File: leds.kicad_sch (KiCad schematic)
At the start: 61 parts, among them U14 ADUM1201ARZ-RL7

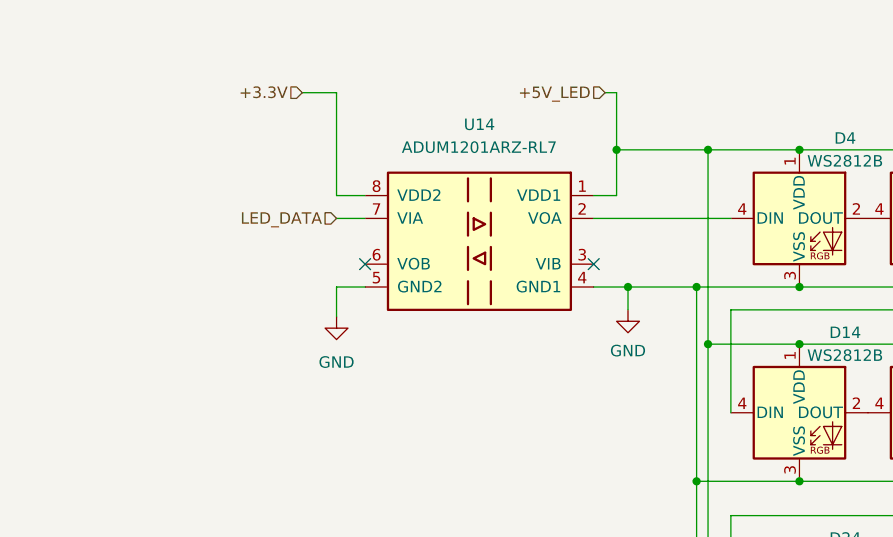
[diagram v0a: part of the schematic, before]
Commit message: bypass caps for digital isolators
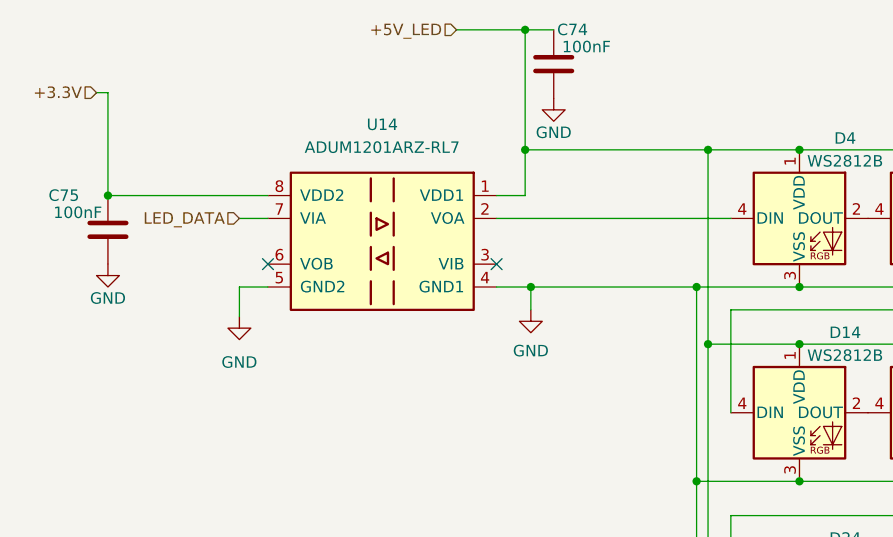
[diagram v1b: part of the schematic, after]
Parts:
- added C74, C75: 100nF, Capacitor_SMD:C_0402_1005Metric, symbol Device:C
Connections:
- net +3.3V: now also C75.2
- net +5V_LED: now also C74.2
- net GND: now also C74.1, C75.1
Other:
- moved on the sheet: U14

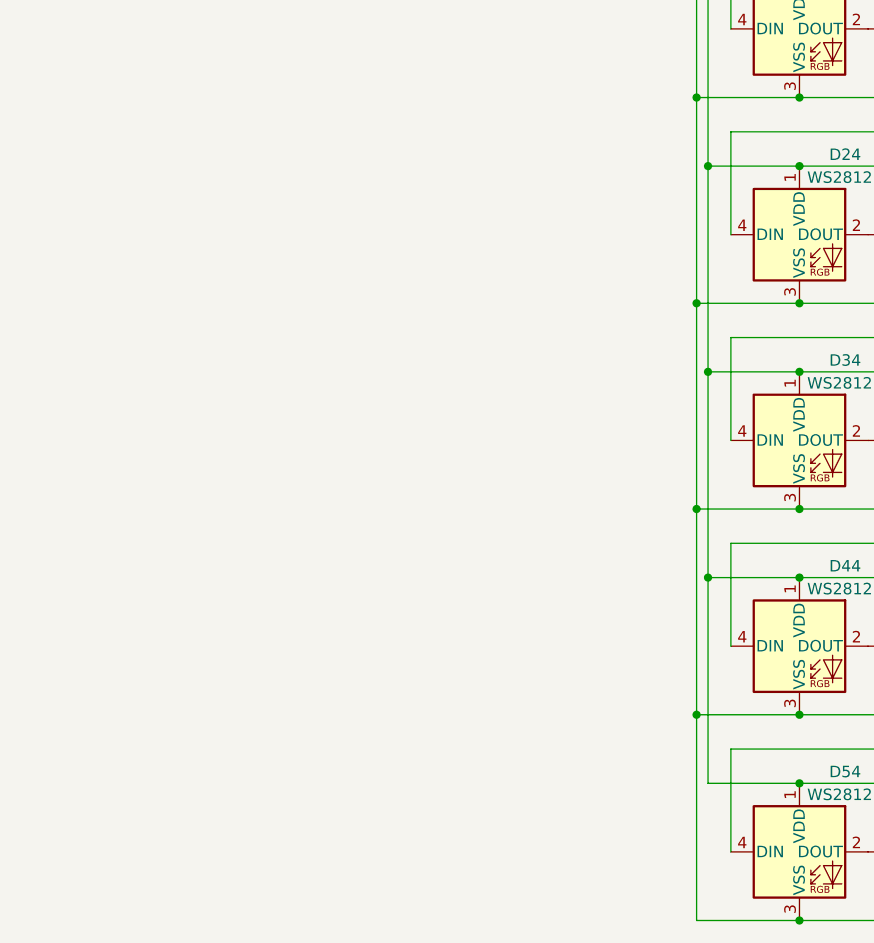
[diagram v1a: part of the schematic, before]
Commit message: first round of routing completed, led capacitors added to schematics
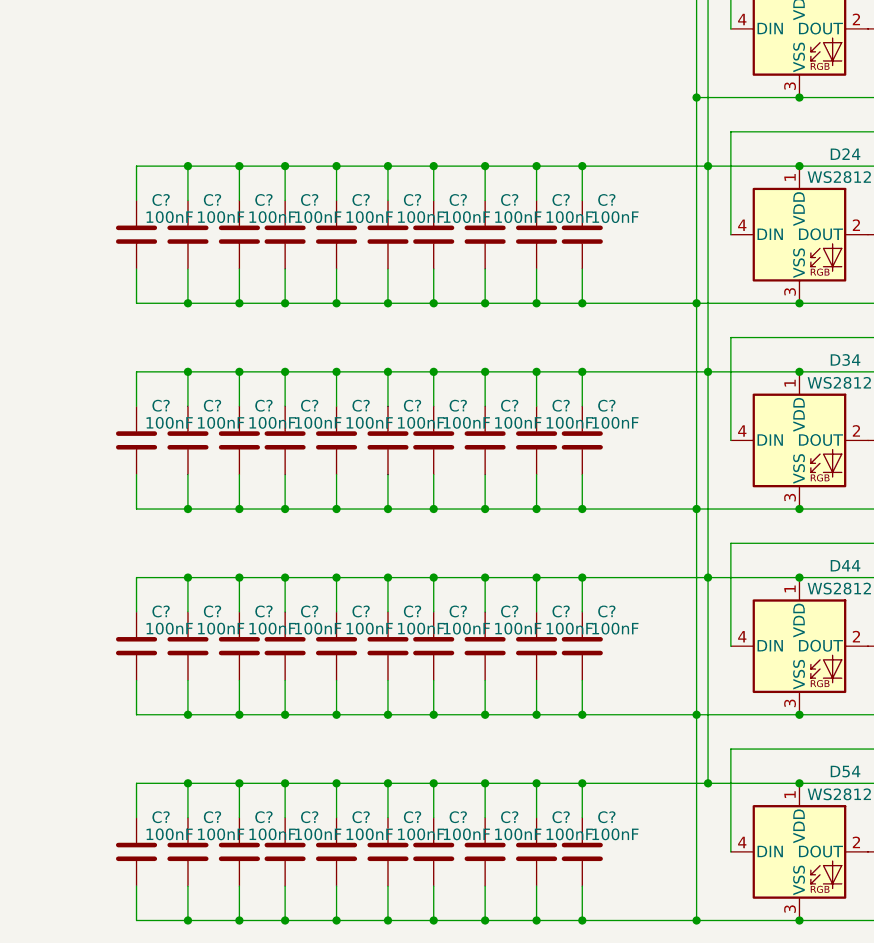
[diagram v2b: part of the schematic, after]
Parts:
- added C? (x40): 100nF, Capacitor_SMD:C_0402_1005Metric, symbol Device:C
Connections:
- net +5V_LED: now also C?.2, C?.2, C?.2, C?.2, C?.2, C?.2, C?.2, C?.2, C?.2, C?.2, C?.2, C?.2, C?.2, C?.2, C?.2, C?.2, C?.2, C?.2, C?.2, C?.2, C?.2, C?.2, C?.2, C?.2, C?.2, C?.2, C?.2, C?.2, C?.2, C?.2, C?.2, C?.2, C?.2, C?.2, C?.2, C?.2, C?.2, C?.2, C?.2, C?.2
- net GND: now also C?.1, C?.1, C?.1, C?.1, C?.1, C?.1, C?.1, C?.1, C?.1, C?.1, C?.1, C?.1, C?.1, C?.1, C?.1, C?.1, C?.1, C?.1, C?.1, C?.1, C?.1, C?.1, C?.1, C?.1, C?.1, C?.1, C?.1, C?.1, C?.1, C?.1, C?.1, C?.1, C?.1, C?.1, C?.1, C?.1, C?.1, C?.1, C?.1, C?.1

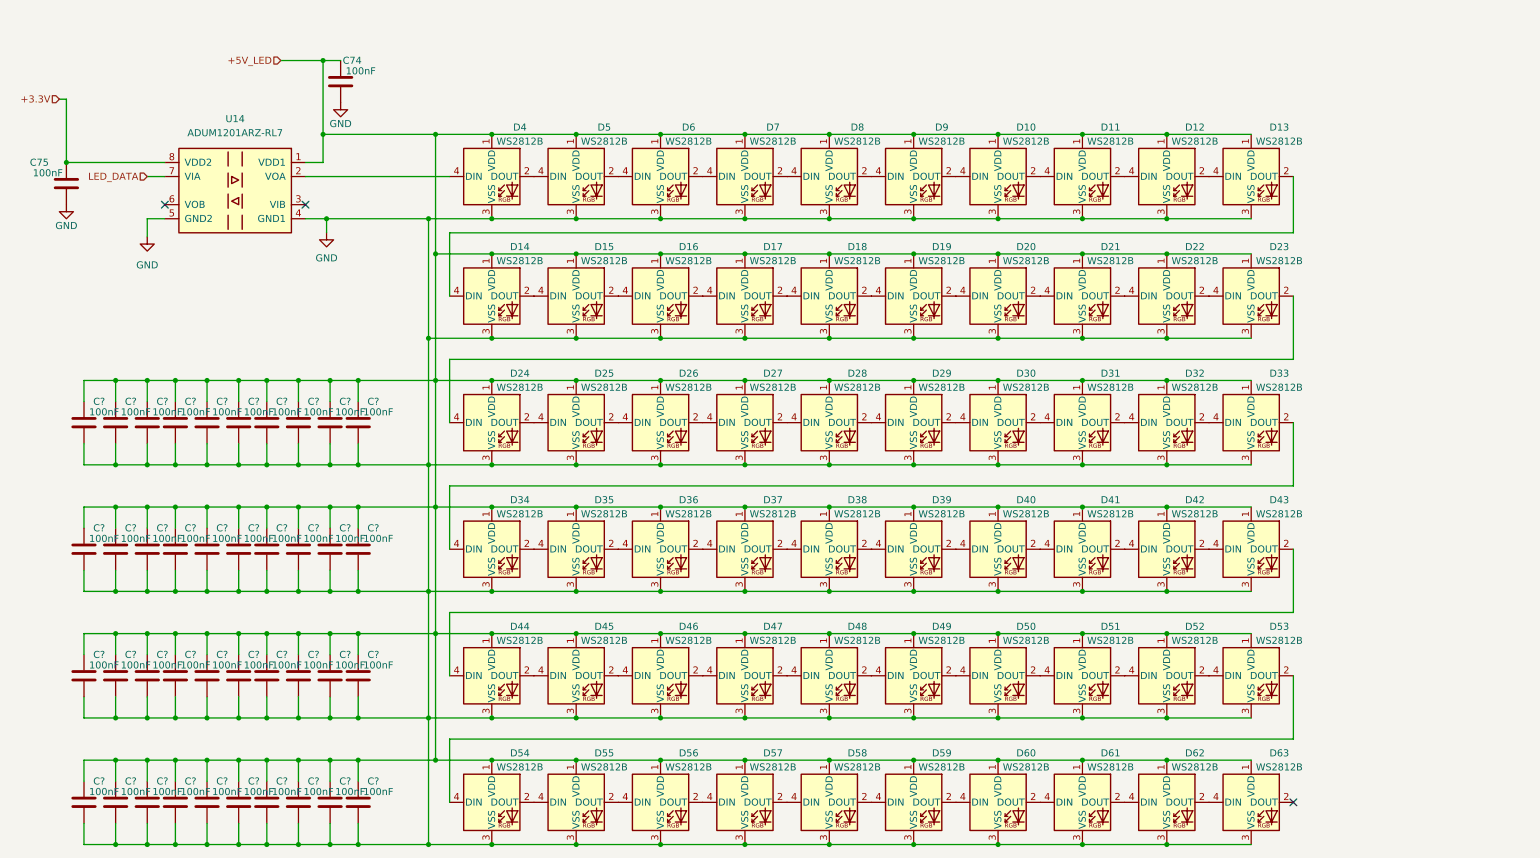
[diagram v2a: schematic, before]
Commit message: led capacitors routed
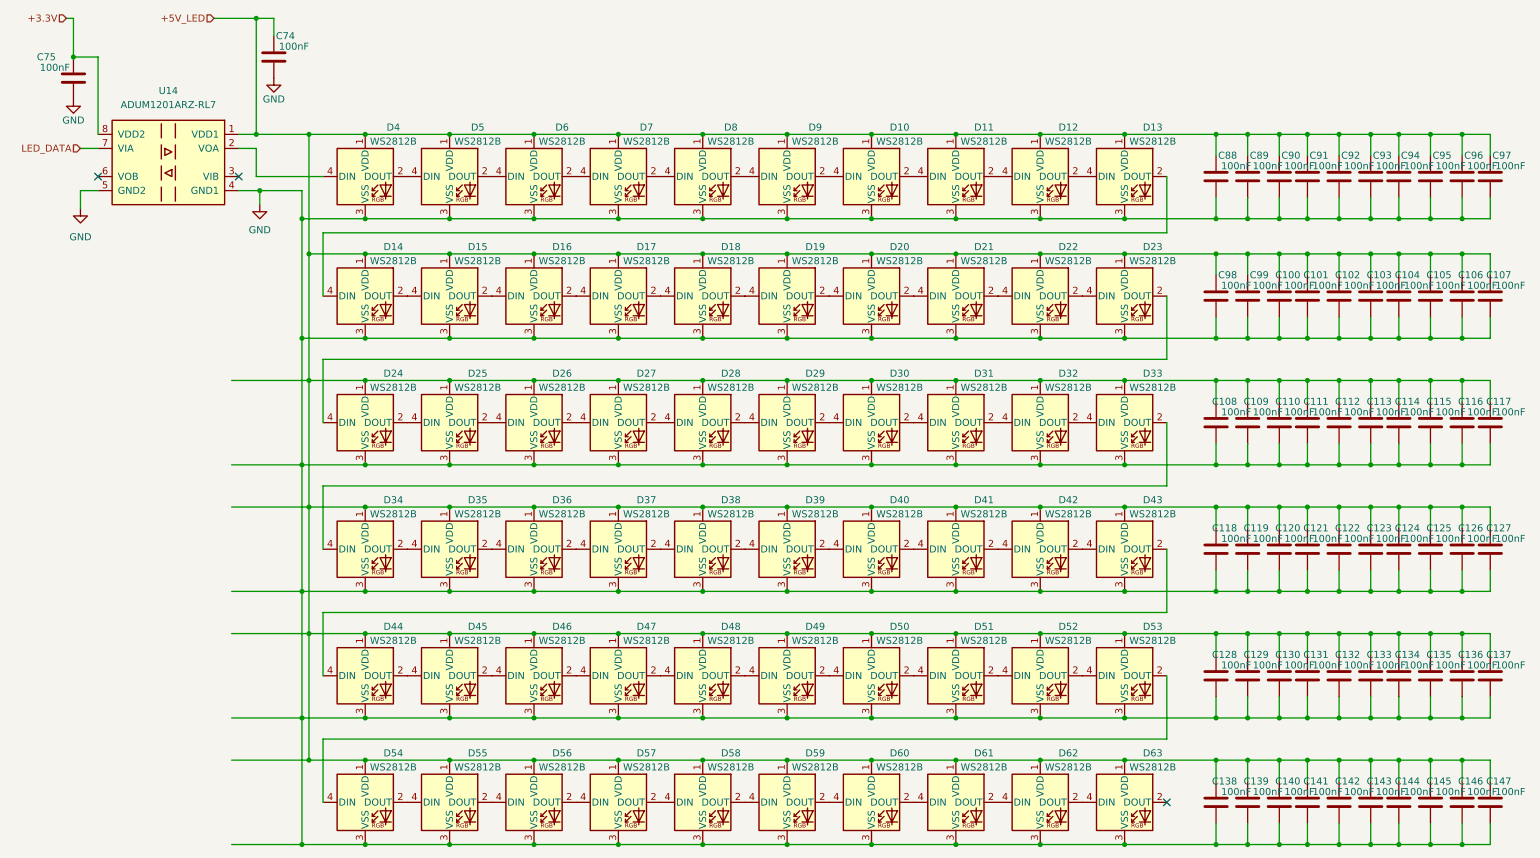
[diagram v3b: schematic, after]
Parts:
- added C128, C129, C130, C131, C132, C133, C134, C135, C136, C137, C138, C139, C140, C141, C142, C143, C144, C145, C146, C147: 100nF, Capacitor_SMD:C_0402_1005Metric, symbol Device:C
- gave numbers to parts that had none: 40
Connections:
- net +5V_LED: now also C128.2, C129.2, C130.2, C131.2, C132.2, C133.2, C134.2, C135.2, C136.2, C137.2, C138.2, C139.2, C140.2, C141.2, C142.2, C143.2, C144.2, C145.2, C146.2, C147.2
- net GND: now also C128.1, C129.1, C130.1, C131.1, C132.1, C133.1, C134.1, C135.1, C136.1, C137.1, C138.1, C139.1, C140.1, C141.1, C142.1, C143.1, C144.1, C145.1, C146.1, C147.1
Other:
- moved on the sheet: C100, C101, C102, C103, C104, C105, C106, C107, C108, C109, C110, C111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

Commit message: more 'LCSC' fields in sch files changed to 'LCSC Part'
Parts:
- C100, C101, C102, C103, C104, C105, C106, C107, C108, C109, C110, C111, C112, C113, C114, C115, C116, C117, C118, C119, C120, C121, C122, C123, C124, C125, C126, C127, C128, C129, C130, C131, C132, C133, C134, C135, C136, C137, C138, C139, C140, C141, C142, C143, C144, C145, C146, C147, C74, C75, C88, C89, C90, C91, C92, C93, C94, C95, C96, C97, C98, C99: LCSC C307331 -> (none); LCSC Part (none) -> C307331
- D10, D11, D12, D13, D14, D15, D16, D17, D18, D19, D20, D21, D22, D23, D24, D25, D26, D27, D28, D29, D30, D31, D32, D33, D34, D35, D36, D37, D38, D39, D4, D40, D41, D42, D43, D44, D45, D46, D47, D48, D49, D5, D50, D51, D52, D53, D54, D55, D56, D57, D58, D59, D6, D60, D61, D62, D63, D7, D8, D9: LCSC C527089 -> (none); LCSC Part (none) -> C527089
- U14: LCSC C9669 -> (none); LCSC Part (none) -> C9669

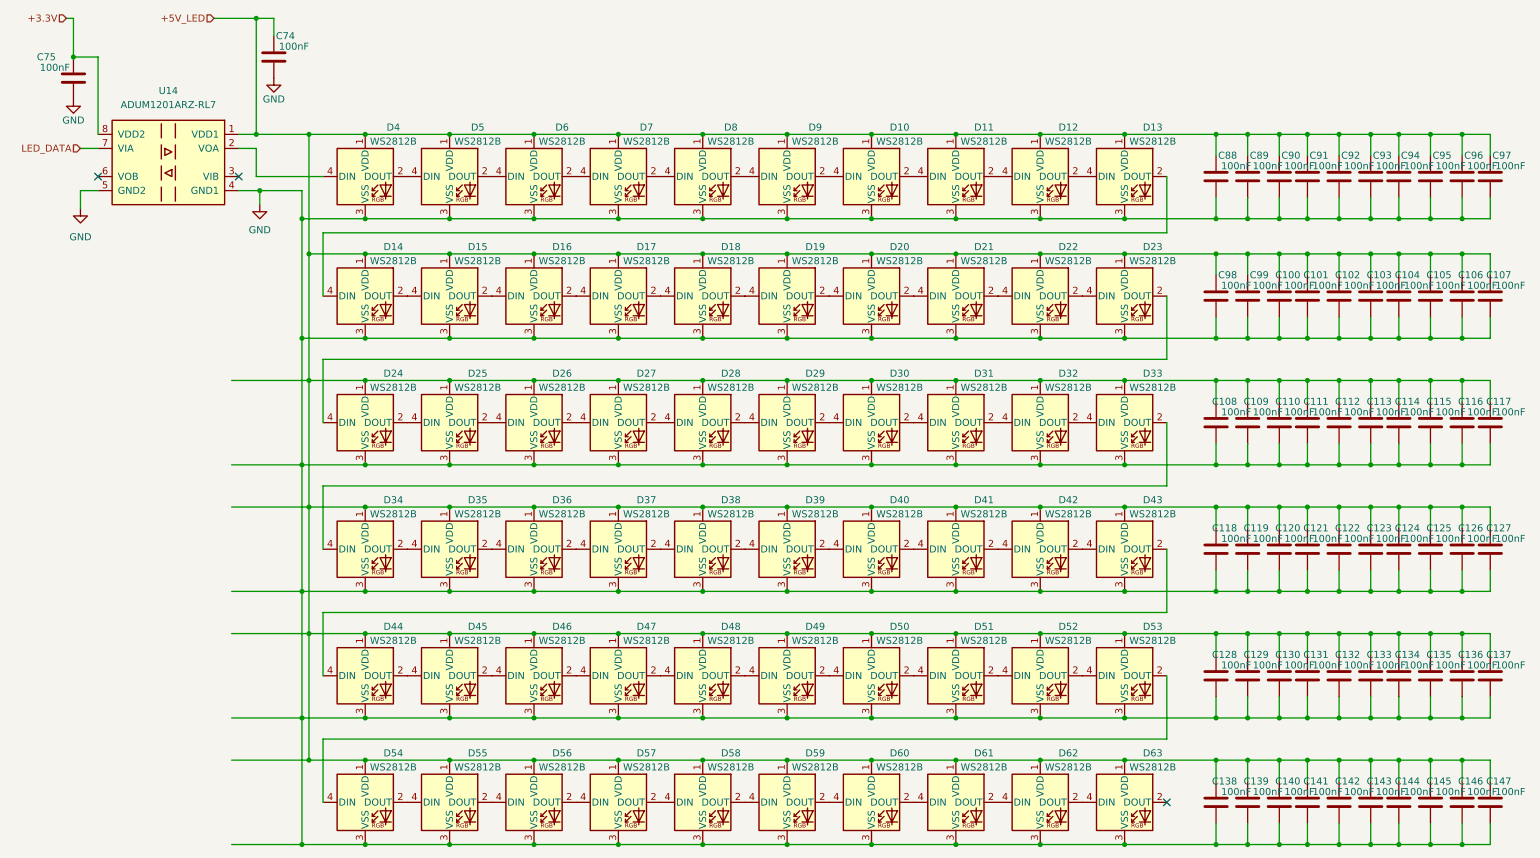
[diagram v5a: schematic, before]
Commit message: resolved align to grid warnings
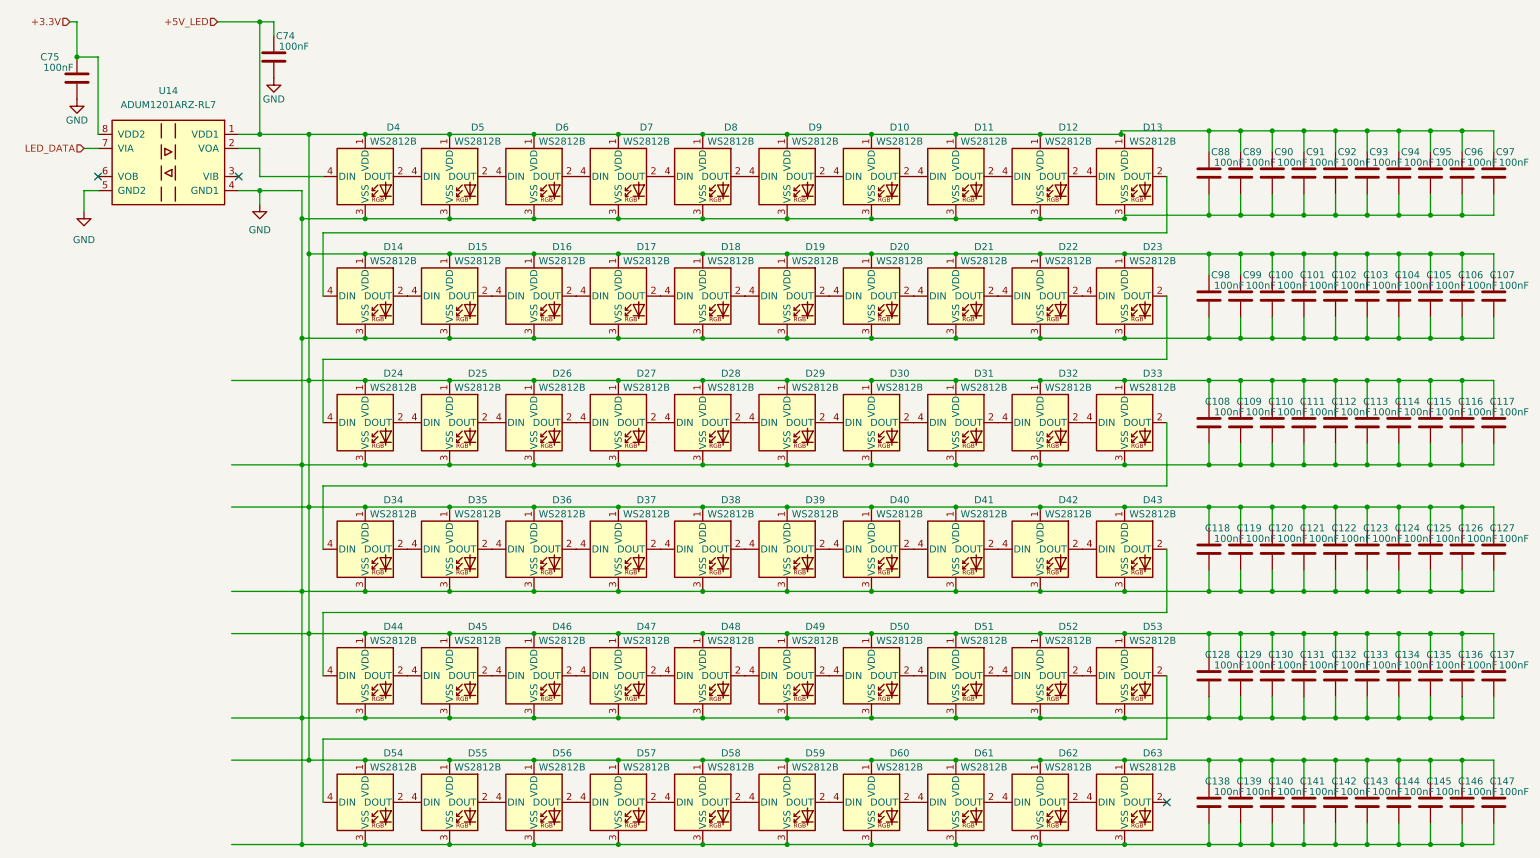
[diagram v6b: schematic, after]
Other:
- moved on the sheet: C100, C101, C102, C103, C107, C108, C109, C110, C111, C112, C113, C117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

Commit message: removed resistors from rotary enc;  aligned mikrobus socket to the center
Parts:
- C74, C75: footprint Capacitor_SMD:C_0402_1005Metric -> Capacitor_SMD:C_0805_2012Metric; LCSC Part C307331 -> C49678
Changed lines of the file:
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@@
       (effects (font (size 1.27 1.27)) (justify left))
     )
-    (property "Footprint" "Capacitor_SMD:C_0402_1005Metric" (at 57.4548 17.78 0)
-      (effects (font (size 1.27 1.27)) hide)
-    )
-    (property "Datasheet" "https://datasheet.lcsc.com/lcsc/1810191222_Samsung-Electro-Mechanics-CL05B104KB54PNC_C307331.pdf" (at 58.42 21.59 0)
-      (effects (font (size 1.27 1.27)) hide)
-    )
-    (property "LCSC Part" "C307331" (at 58.42 21.59 0)
+    (property "Footprint" "Capacitor_SMD:C_0805_2012Metric" (at 57.4548 17.78 0)
+      (effects (font (size 1.27 1.27)) hide)
+    )
+    (property "Datasheet" "https://datasheet.lcsc.com/lcsc/1810101813_YAGEO-CC0805KRX7R9BB104_C49678.pdf" (at 58.42 21.59 0)
+      (effects (font (size 1.27 1.27)) hide)
+    )
+    (property "LCSC Part" "C49678" (at 58.42 21.59 0)
       (effects (font (size 1.27 1.27)) hide)
     )
@@
       (effects (font (size 1.27 1.27)) (justify left))
     )
-    (property "Footprint" "Capacitor_SMD:C_0402_1005Metric" (at 21.8948 21.59 0)
-      (effects (font (size 1.27 1.27)) hide)
-    )
-    (property "Datasheet" "https://datasheet.lcsc.com/lcsc/1810191222_Samsung-Electro-Mechanics-CL05B104KB54PNC_C307331.pdf" (at 22.86 25.4 0)
-      (effects (font (size 1.27 1.27)) hide)
-    )
-    (property "LCSC Part" "C307331" (at 22.86 25.4 0)
-      (effects (font (size 1.27 1.27)) hide)
-    )
+    (property "Footprint" "Capacitor_SMD:C_0805_2012Metric" (at 21.8948 21.59 0)
+      (effects (font (size 1.27 1.27)) hide)
+    )
+    (property "Datasheet" "https://datasheet.lcsc.com/lcsc/1810101813_YAGEO-CC0805KRX7R9BB104_C49678.pdf" (at 22.86 25.4 0)
+      (effects (font (size 1.27 1.27)) hide)
+    )
+    (property "LCSC Part" "C49678" (at 22.86 25.4 0)
+      (effects (font (size 1.27 1.27)) hide)
+    )
